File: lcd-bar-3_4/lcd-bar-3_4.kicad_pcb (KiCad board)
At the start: 2 copper layers, 85 x 36 mm, 32 parts, among them J1 SWD, J2 Conn_01x40_MountingPin, SW1 BOOT0, SW2 RST, U1 siplex-som-s16, U2 TPS61169

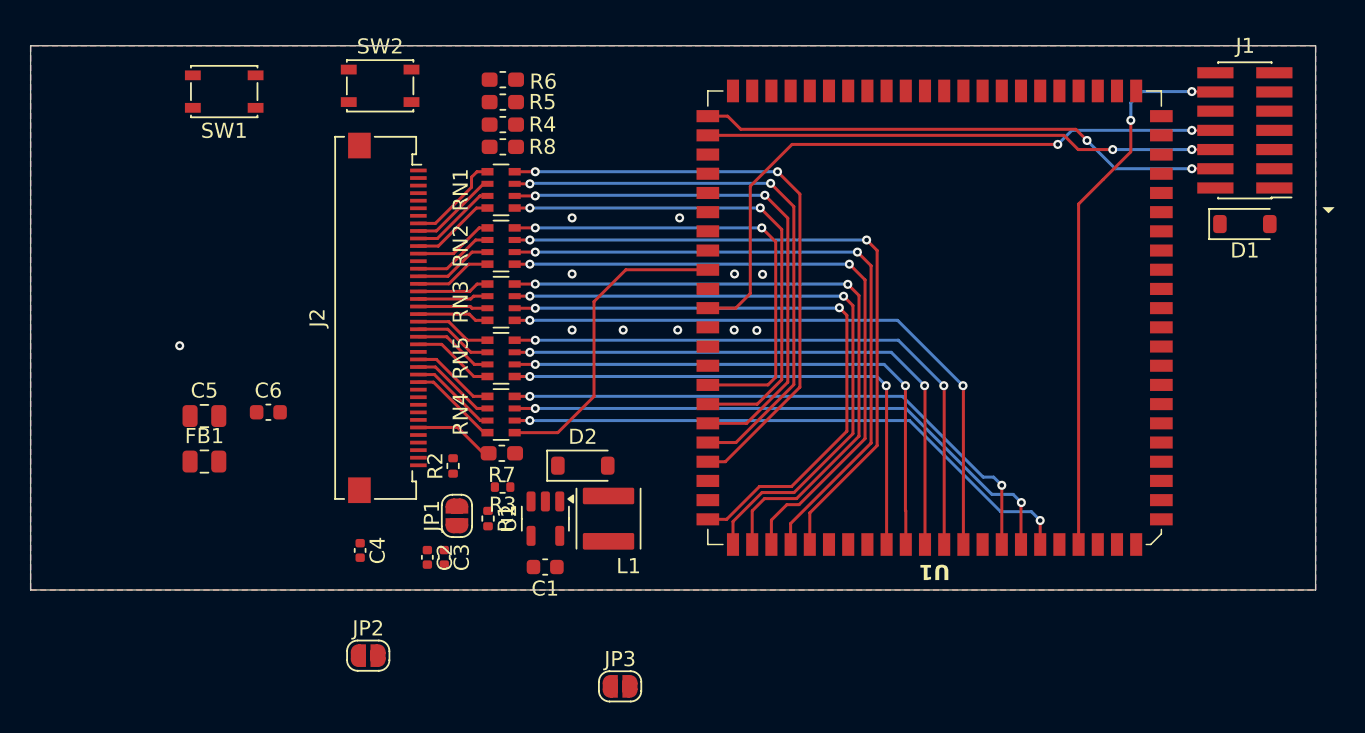
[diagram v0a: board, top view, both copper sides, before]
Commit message: Add LCD square 4-inch 480-480 & 720-720
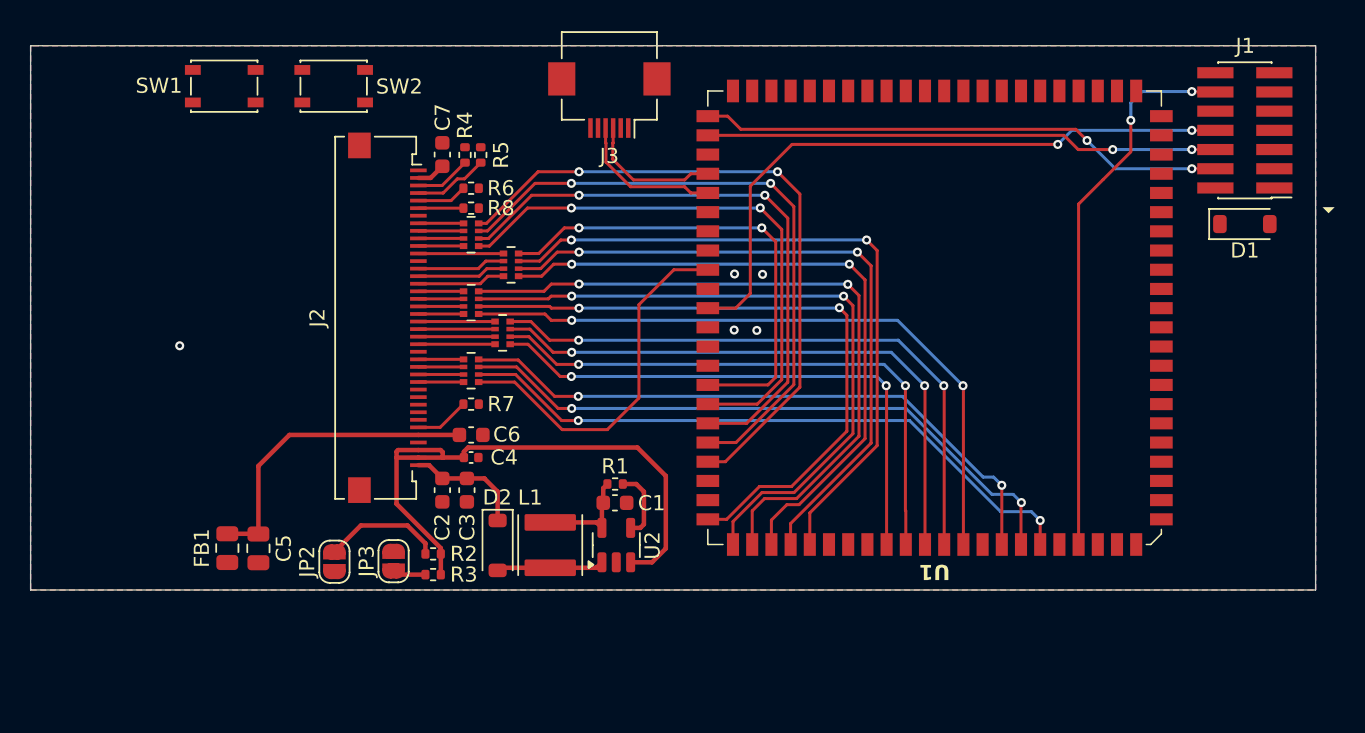
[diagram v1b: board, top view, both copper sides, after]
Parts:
- removed JP1: JMP, Jumper:SolderJumper-2_P1.3mm_Open_RoundedPad1.0x1.5mm
- added C7: 100n, Capacitor_SMD:C_0603_1608Metric, F.Cu at (120.2, 83.8)
- added J3: Conn_01x06_MountingPin, Connector_FFC-FPC:Hirose_FH12-6S-0.5SH_1x06-1MP_P0.50mm_Horizontal, F.Cu at (131.3, 80.2)
- C2, C3: footprint Capacitor_SMD:C_0402_1005Metric -> Capacitor_SMD:C_0603_1608Metric
- R4, R5, R6, R7, R8: footprint Inductor_SMD:L_0603_1608Metric_Pad1.05x0.95mm_HandSolder -> Resistor_SMD:R_0402_1005Metric
- RN1, RN2, RN3, RN4, RN5: footprint Resistor_SMD:R_Array_Convex_4x0603 -> Resistor_SMD:R_Array_Convex_4x0402
- moved JP3 17.1 mm to (117.0, 110.7), turned to -90 degrees
- moved C6 13.5 mm to (122.1, 102.3)
- moved C4 9.57 mm to (122.1, 103.8), turned to 0 degrees
- moved C5 9.45 mm to (108.1, 109.8), turned to -90 degrees
- moved R1 8.71 mm to (131.6, 105.6), turned to 0 degrees
- moved D2 7.72 mm to (123.9, 109.6), turned to -90 degrees
- moved R6 7.48 mm to (122.1, 86.0)
- moved R3 7.39 mm to (119.6, 111.6)
- moved JP2 6.60 mm to (113.1, 110.7), turned to 90 degrees
- moved C1 6.27 mm to (131.6, 106.8), turned to 0 degrees
- moved R2 5.96 mm to (119.6, 110.2), turned to 180 degrees
- moved FB1 5.92 mm to (106.0, 109.8), turned to 90 degrees
- moved U2 5.00 mm to (131.7, 109.6), turned to 90 degrees
- moved C3 4.69 mm to (121.8, 106.0)
- moved R8 4.56 mm to (122.1, 87.3)
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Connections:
- R1 pad 2: Net-(JP1-B) -> /LCD_BLK
- U2 pad 4: Net-(JP1-B) -> /LCD_BLK
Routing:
- net /LED_K: track 0.00 -> 39.5 mm
- net VDD_LCD: track 0.00 -> 20.7 mm
- net /USB_DP: track 0.00 -> 9.85 mm
- net /USB_DN: track 0.00 -> 9.10 mm
- net Net-(JP2-B): track 0.00 -> 7.93 mm
- net /LED_A: track 0.00 -> 7.87 mm
- net Net-(D2-A): track 0.00 -> 7.12 mm
- net +5V: track 0.00 -> 6.62 mm
- net /LCD_TP_SCL: track 0.00 -> 4.96 mm
- net /LCD_BLK: track 0.00 -> 4.74 mm
- net /R7: track 40.4 -> 44.2 mm
- net /LCD_TP_RST: track 0.00 -> 3.71 mm
- net /R6: track 38.2 -> 41.8 mm
- net Net-(RN4-R3.2): track 39.1 -> 42.7 mm
- net /R5: track 36.0 -> 39.5 mm
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
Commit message: 98% finished, st-link part left
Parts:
- added J4: Conn_01x10_MountingPin, Connector_Molex:Molex_PicoBlade_53261-1071_1x10-1MP_P1.25mm_Horizontal, F.Cu at (173.5, 102.1)
- moved R7 20.8 mm to (103.8, 110.2), turned to 90 degrees
- moved C1 0.63 mm to (131.6, 106.2)
- moved D2 0.63 mm to (123.9, 109.0)
- moved L1 0.63 mm to (127.3, 109.0)
- moved R1 0.63 mm to (131.6, 104.9), turned to 180 degrees
- moved U2 0.63 mm to (131.7, 109.0)
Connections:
- net Net-(D2-A) renamed /SW
- R1 pad 1: +5V -> /LCD_BLK
- R1 pad 2: /LCD_BLK -> GND
- U1 pad 1: /LCD_RST -> /LCD_TP_INT
- U1 pad 10: unconnected-(U1-PA1-Pad10) -> /PWR_BTN
- U1 pad 16: unconnected-(U1-PB0-Pad16) -> /LCD_BLK
- U1 pad 20: unconnected-(U1-PB10-Pad20) -> /EE_SCL
- U1 pad 22: unconnected-(U1-PB11-Pad22) -> /EE_SDA
- U1 pad 23: unconnected-(U1-PB14-Pad23) -> /SERIAL_TX
- U1 pad 24: unconnected-(U1-PB15-Pad24) -> /SERIAL_RX
- U1 pad 35: unconnected-(U1-PD7-Pad35) -> /LCD_SPI_DAT
- U1 pad 36: unconnected-(U1-PI3-Pad36) -> /LCD_RST
- U1 pad 38: unconnected-(U1-PC12-Pad38) -> /LCD_SPI_CS
- U1 pad 4: /LCD_TP_INT -> /LCD_TP_RST
- U1 pad 40: /LCD_SPI_CS -> unconnected-(U1-PB4-Pad40)
- U1 pad 6: /LCD_TP_RST -> /AUX_IO
- U1 pad 88: /LCD_SPI_DAT -> unconnected-(U1-PB5-Pad88)
- U1 pad 9: unconnected-(U1-PA0-Pad9) -> /PWR_LED
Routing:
- net +3V3: track 1.90 -> 147.6 mm, vias 0 -> 8
- net +5V: track 6.62 -> 116.6 mm, vias 0 -> 7
- net /BOOT0: track 0.00 -> 96.4 mm, vias 0 -> 2
- net /RESET: track 36.6 -> 132.5 mm, vias 2 -> 4
- net /LCD_RST: track 3.62 -> 70.7 mm, vias 0 -> 2
- net /LCD_BLK: track 4.74 -> 67.5 mm, vias 0 -> 2
- net /LCD_TP_RST: track 3.71 -> 61.5 mm, vias 0 -> 2
- net /LCD_TP_SDA: track 3.32 -> 59.3 mm, vias 0 -> 2
- net /LCD_TP_INT: track 2.98 -> 58.7 mm, vias 0 -> 2
- net /LCD_TP_SCL: track 4.96 -> 59.2 mm, vias 0 -> 2
- net /LCD_SPI_DAT: track 0.00 -> 54.0 mm, vias 0 -> 2
- net /LCD_SPI_CLK: track 0.00 -> 45.7 mm, vias 0 -> 2
- net /LCD_SPI_CS: track 0.00 -> 44.9 mm, vias 0 -> 2
- net /SERIAL_RX: track 0.00 -> 25.9 mm, vias 0 -> 2
- net /SERIAL_TX: track 0.00 -> 24.5 mm, vias 0 -> 2
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- added copper zone on B.Cu, net +5V
- added copper zone on F.Cu, net +5V
- added copper zone on B.Cu, net /SW
- added copper zone on F.Cu, net /SW
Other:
- outline, holes or cut-outs redrawn
- board text added: "15mA"
- board text added: "30mA"
- board text added: "BOOT"
- board text added: "RESET"

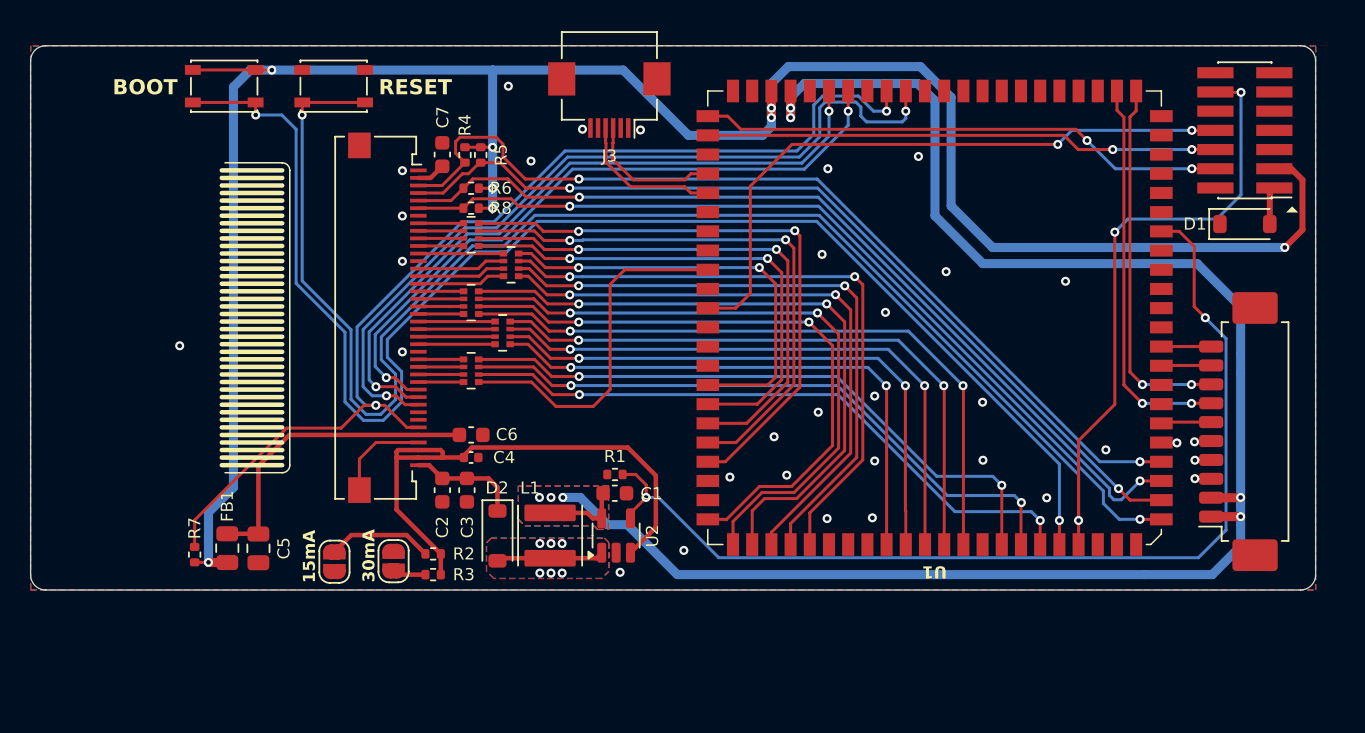
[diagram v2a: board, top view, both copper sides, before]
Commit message: Add LCD standard 7inch
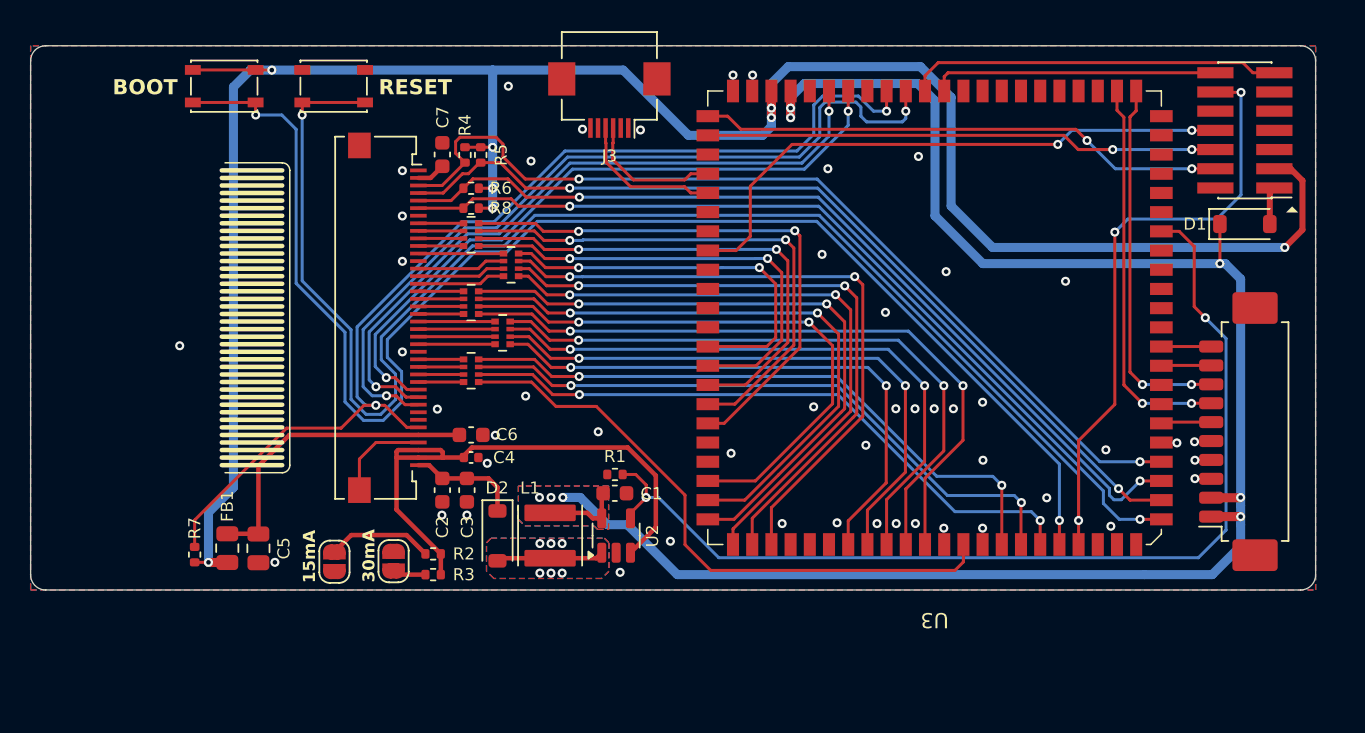
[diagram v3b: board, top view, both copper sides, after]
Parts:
- removed U1: siplex-som-s16, siplex:siplex-som-s16
- added U3: siplex-som-s16, siplex:siplex-som-s16, F.Cu at (152.8, 94.6)
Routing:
- net /VCP_RX: track 0.00 -> 24.7 mm
- net /VCP_TX: track 0.00 -> 19.0 mm
- net Net-(RN4-R4.2): track 23.6 -> 40.5 mm
- net /SWO: track 42.6 -> 38.8 mm
- net +5V: track 116.6 -> 120.3 mm, vias 7 -> 8
- net /G2: track 41.4 -> 38.7 mm
- net /R7: track 39.8 -> 37.2 mm
- net /R4: track 33.4 -> 30.8 mm
- net /R3: track 28.7 -> 26.1 mm
- net /R6: track 37.7 -> 35.1 mm
- net /R5: track 35.5 -> 32.9 mm
- net /G3: track 42.8 -> 40.8 mm
- net /B3: track 36.5 -> 37.6 mm
- net /B7: track 44.5 -> 45.6 mm
- net /B6: track 41.0 -> 42.0 mm
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
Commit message: Slight changes
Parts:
- C1: footprint Capacitor_SMD:C_0603_1608Metric -> Capacitor_SMD:C_0805_2012Metric
- C6, C7: footprint Capacitor_SMD:C_0603_1608Metric -> Capacitor_SMD:C_0402_1005Metric
- RN1, RN2, RN3, RN4, RN5: value 22 -> 100
- moved C1 1.79 mm to (130.5, 104.8), turned to 90 degrees
- moved R1 1.08 mm to (132.7, 105.3), turned to 90 degrees
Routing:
- net +3V3: track 147.6 -> 151.8 mm, vias 8 -> 9
- net Net-(RN4-R4.2): track 40.5 -> 41.8 mm
- net /LED_K: track 36.9 -> 37.5 mm
